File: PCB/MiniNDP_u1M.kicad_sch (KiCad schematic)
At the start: 12 parts, among them J1 Model_100_System_BUS, U1 AS6C8008_TSOPII, U2 HC238, U3 HC4040, U4 ABT841

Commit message: Olivetti M-10 take 3. T512 pics readme.
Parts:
- U4: footprint 000_LOCAL:TSSOP-24_4.4x7.8mm_P0.65mm -> 000_LOCAL:TSSOP-24
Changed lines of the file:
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@@
 			)
 		)
-		(property "Footprint" "000_LOCAL:TSSOP-24_4.4x7.8mm_P0.65mm"
+		(property "Footprint" "000_LOCAL:TSSOP-24"
 			(at 146.05 101.6 0)
 			(effects

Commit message: add sram part numbers to 1M versions sch
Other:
- note added: "AS6C8008-xxZ CY62158ELL"
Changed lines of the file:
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@@
 		(comment 2 "1M RAM Disk for TRS-80 Model 100")
+	)
+	(text "AS6C8008-xxZ\nCY62158ELL"
+		(exclude_from_sim no)
+		(at 222.25 22.86 0)
+		(effects
+			(font
+				(size 1.27 1.27)
+			)
+		)
 	)
 	(text "		BUS  BUS  BUS  BUS\n(A)	~{YO}   _A8  _A9  _A10  _A11  ->  ~{BLOCK} ~{BYTE}\n L	 X	 X	  X	  X	   X		X	  X\n X	 H	 X	  X	  X	   X		X	  X\n X	 X	 L	  X	  X	   X		X	  X\n H	 L	 H	  L	  L	   L	->  H	  L  Select BLOCK N, BANK0: OUT129,N\n H	 L	 H	  L	  H	   L	->  H	  L  Select BLOCK N, BANK1: OUT133,N\n H	 L	 H	  L	  L	   H	->  H	  L  Select BLOCK N, BANK2: OUT137,N\n H	 L	 H	  L	  H	   H	->  H	  L  Select BLOCK N, BANK3: OUT141,N\n H	 L	 H	  H	  X	   X	->  L	  H  READ N: N=INP(131) or WRITE N: OUT131,N\n\nBLOCK\nH: sets A0-A9 to 0, updates A10-A19 from AD0-AD7 & BUS_A10-BUS_A11\nL: latches A10-A19\n\nBYTE\nH: enables SRAM for read or write\nL: disables SRAM, increments A0-A9 by 1\n"

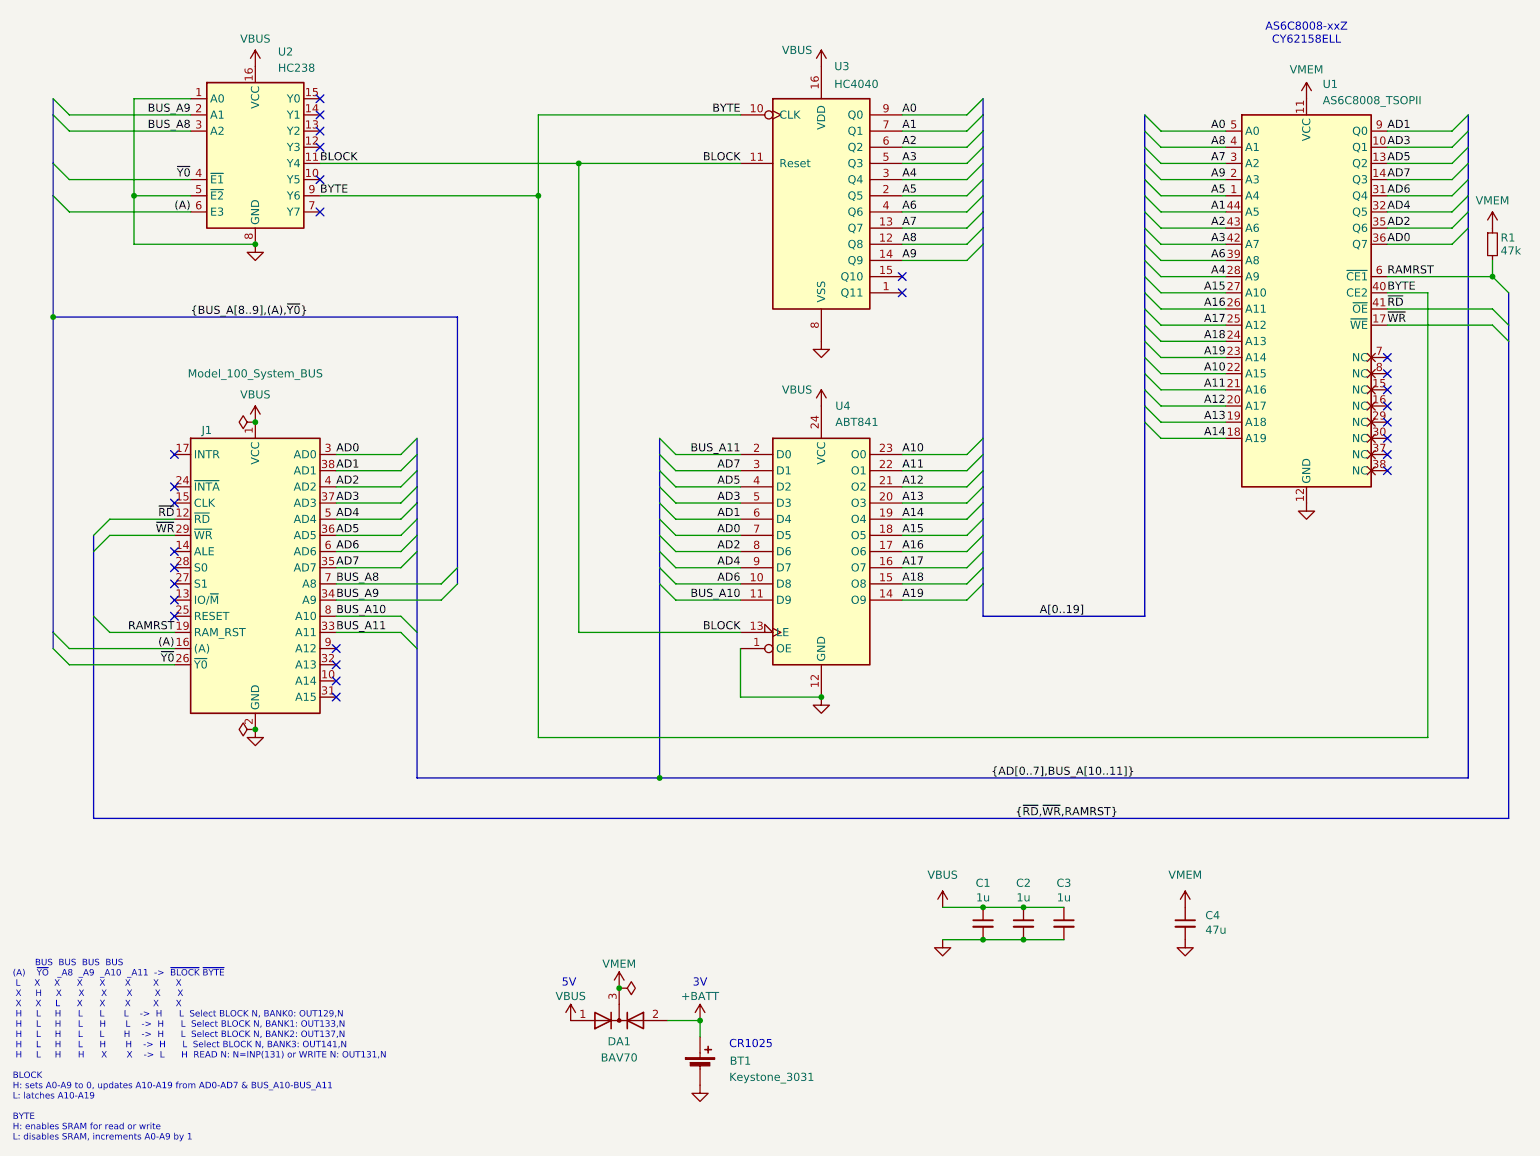
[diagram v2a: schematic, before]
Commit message: simplify covers, strengthen battery holders, silkscreen, readme
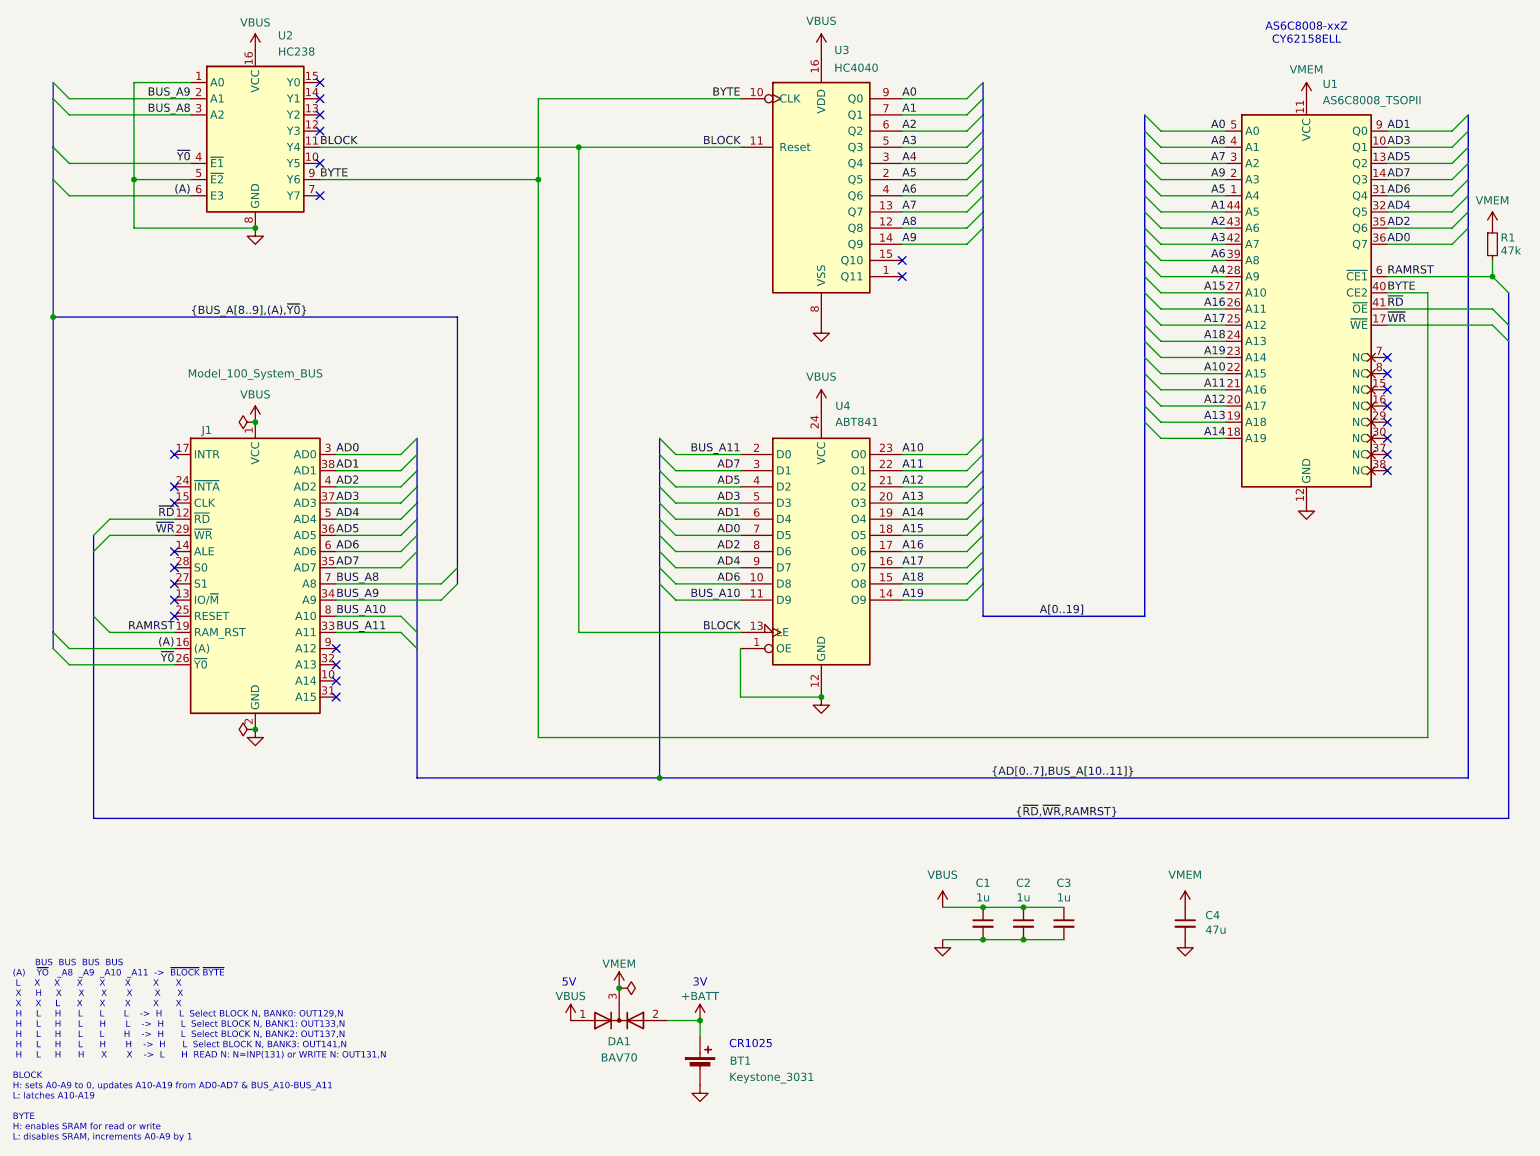
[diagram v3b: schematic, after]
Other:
- moved on the sheet: U2, U3
